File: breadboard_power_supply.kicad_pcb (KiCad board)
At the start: 2 copper layers, 75.2 x 54.4 mm, 25 parts, among them J1 PJ-059AH, J10 Conn_01x04, J11 Conn_01x12, J12 Conn_01x04, J13 Conn_01x04, J14 Conn_01x04, J2 Conn_01x07, J3 Conn_01x08, J4 Screw_Terminal_01x06, J5 Conn_01x04_Male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

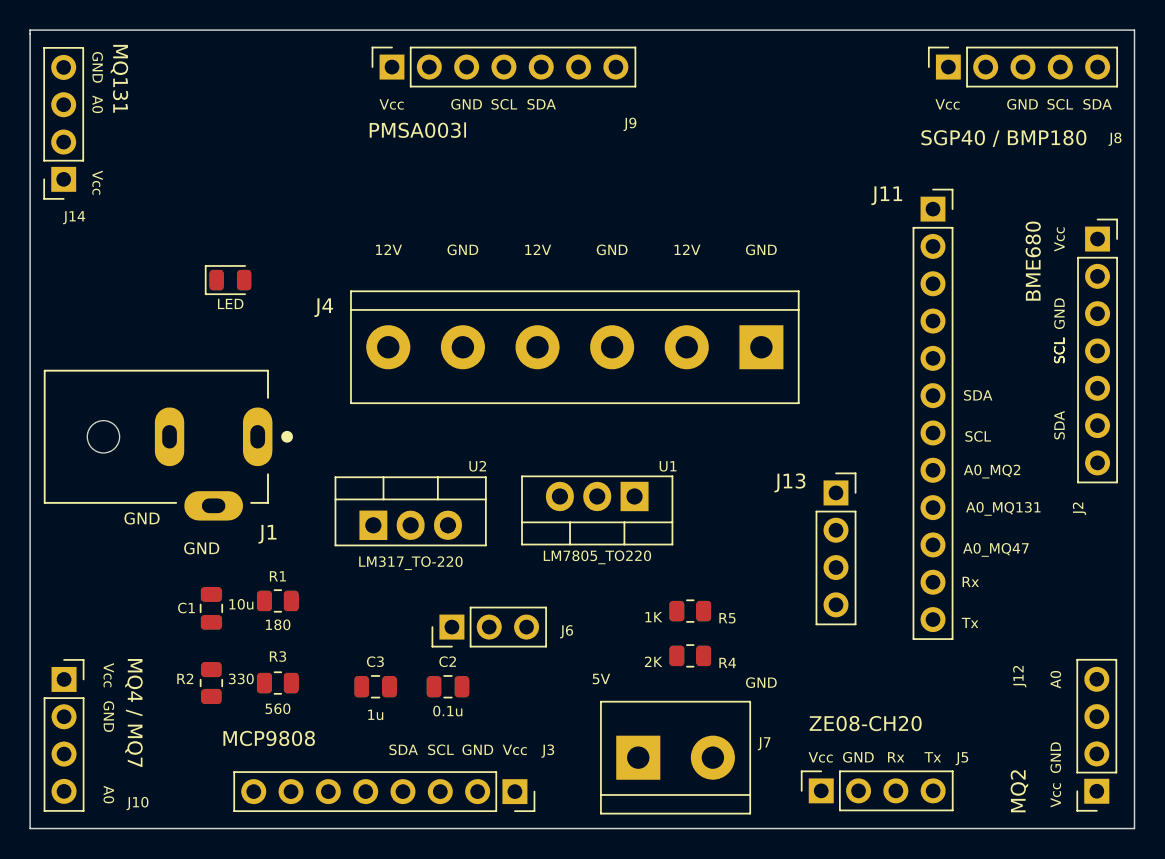
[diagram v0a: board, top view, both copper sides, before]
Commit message: Remaining : route tracking
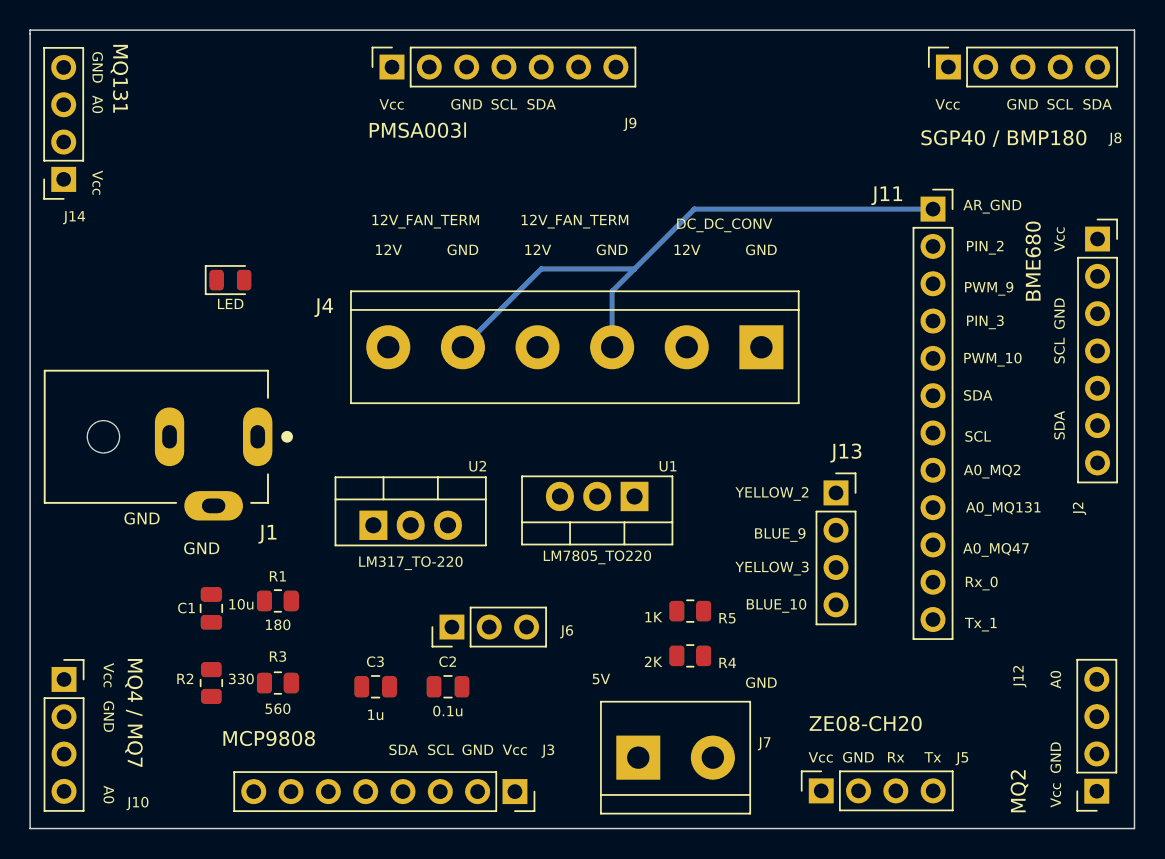
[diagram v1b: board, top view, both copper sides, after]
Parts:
- J11: value Conn_01x12 -> Conn_01x12_Male
- J13: value Conn_01x04 -> Conn_01x04_Male
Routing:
- net GND: track 0.00 -> 41.9 mm
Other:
- board text added: "12V_FAN_TERM"
- board text added: "AR_GND"
- board text added: "BLUE_10"
- board text added: "BLUE_9"
- board text added: "DC_DC_CONV"
- board text added: "PIN_2"
- board text added: "PIN_3"
- board text added: "PWM_10"
- board text added: "PWM_9"
- board text added: "Rx_0"
- board text added: "Tx_1"
- board text added: "YELLOW_2"
- board text added: "YELLOW_3"
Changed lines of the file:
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@@
       (effects (font (size 1 1) (thickness 0.15)))
     )
-    (fp_text value "Conn_01x12" (at -2.794 22.865 90) (layer "F.Fab")
+    (fp_text value "Conn_01x12_Male" (at -2.794 22.865 90) (layer "F.Fab")
       (effects (font (size 1 1) (thickness 0.15)))
     )
@@
     (property "Sheetname" "")
     (attr through_hole)
-    (fp_text reference "J13" (at -3.048 -0.772) (layer "F.SilkS")
-      (effects (font (size 1 1) (thickness 0.15)))
-    )
-    (fp_text value "Conn_01x04" (at -2.794 3.292 90) (layer "F.Fab")
+    (fp_text reference "J13" (at 0.762 -2.804) (layer "F.SilkS")
+      (effects (font (size 1 1) (thickness 0.15)))
+    )
+    (fp_text value "Conn_01x04_Male" (at 2.54 3.546 90) (layer "F.Fab")
       (effects (font (size 1 1) (thickness 0.15)))
     )
@@
   (gr_line (start 55.372 117.19) (end 55.372 65.628) (layer "User.1") (width 0.15))
   (gr_line (start 56.114 117.19) (end 55.372 117.19) (layer "User.1") (width 0.15))
+  (gr_text "YELLOW_2" (at 91.948 143.256) (layer "F.SilkS")
+    (effects (font (size 0.7 0.7) (thickness 0.1)))
+  )
   (gr_text "SDA" (at 114.046 116.84) (layer "F.SilkS")
     (effects (font (size 0.7 0.7) (thickness 0.1)))
   )
+  (gr_text "YELLOW_3" (at 91.948 148.336) (layer "F.SilkS")
+    (effects (font (size 0.7 0.7) (thickness 0.1)))
+  )
   (gr_text "SCL" (at 105.918 139.446) (layer "F.SilkS")
     (effects (font (size 0.7 0.7) (thickness 0.1)))
@@
     (effects (font (size 0.7 0.7) (thickness 0.1)))
   )
+  (gr_text "12V_FAN_TERM" (at 78.486 124.714) (layer "F.SilkS")
+    (effects (font (size 0.7 0.7) (thickness 0.1)))
+  )
   (gr_text "Vcc" (at 111.506 125.984 90) (layer "F.SilkS")
     (effects (font (size 0.7 0.7) (thickness 0.1)))
   )
   (gr_text "Rx" (at 100.33 161.29) (layer "F.SilkS")
+    (effects (font (size 0.7 0.7) (thickness 0.1)))
+  )
+  (gr_text "12V_FAN_TERM" (at 68.326 124.714) (layer "F.SilkS")
     (effects (font (size 0.7 0.7) (thickness 0.1)))
   )
@@
     (effects (font (size 0.7 0.7) (thickness 0.1)))
   )
-  (gr_text "Tx" (at 105.41 152.146) (layer "F.SilkS")
+  (gr_text "Tx_1" (at 106.172 152.146) (layer "F.SilkS")
     (effects (font (size 0.7 0.7) (thickness 0.1)))
   )
@@
     (effects (font (size 0.7 0.7) (thickness 0.1)))
   )
+  (gr_text "PIN_3" (at 106.426 131.572) (layer "F.SilkS")
+    (effects (font (size 0.7 0.7) (thickness 0.1)))
+  )
+  (gr_text "PIN_2" (at 106.426 126.492) (layer "F.SilkS")
+    (effects (font (size 0.7 0.7) (thickness 0.1)))
+  )
   (gr_text "12V" (at 65.786 126.746) (layer "F.SilkS")
     (effects (font (size 0.7 0.7) (thickness 0.1)))
@@
     (effects (font (size 0.7 0.7) (thickness 0.1)))
   )
+  (gr_text "DC_DC_CONV" (at 88.646 124.968) (layer "F.SilkS")
+    (effects (font (size 0.7 0.7) (thickness 0.1)))
+  )
   (gr_text "GND" (at 111.252 161.29 90) (layer "F.SilkS")
     (effects (font (size 0.7 0.7) (thickness 0.1)))
@@
     (effects (font (size 0.7 0.7) (thickness 0.1)))
   )
+  (gr_text "BLUE_10" (at 92.202 150.876) (layer "F.SilkS")
+    (effects (font (size 0.7 0.7) (thickness 0.1)))
+  )
   (gr_text "GND" (at 97.79 161.29) (layer "F.SilkS")
     (effects (font (size 0.7 0.7) (thickness 0.1)))
@@
     (effects (font (size 0.7 0.7) (thickness 0.1)))
   )
-  (gr_text "Rx" (at 105.41 149.352) (layer "F.SilkS")
+  (gr_text "Rx_0" (at 106.172 149.352) (layer "F.SilkS")
     (effects (font (size 0.7 0.7) (thickness 0.1)))
   )
@@
     (effects (font (size 0.7 0.7) (thickness 0.1)))
   )
+  (gr_text "PWM_9" (at 106.68 129.286) (layer "F.SilkS")
+    (effects (font (size 0.7 0.7) (thickness 0.1)))
+  )
+  (gr_text "AR_GND" (at 106.934 123.698) (layer "F.SilkS")
+    (effects (font (size 0.7 0.7) (thickness 0.1)))
+  )
   (gr_text "5V" (at 80.264 155.956) (layer "F.SilkS")
     (effects (font (size 0.7 0.7) (thickness 0.1)))
   )
   (gr_text "Vcc" (at 95.25 161.29) (layer "F.SilkS")
-    (effects (font (size 0.7 0.7) (thickness 0.1)))
-  )
-  (gr_text "SCL" (at 111.488305 133.579759 90) (layer "F.SilkS")
     (effects (font (size 0.7 0.7) (thickness 0.1)))
   )
@@
     (effects (font (size 0.7 0.7) (thickness 0.1)))
   )
+  (gr_text "BLUE_9" (at 92.456 146.05) (layer "F.SilkS")
+    (effects (font (size 0.7 0.7) (thickness 0.1)))
+  )
   (gr_text "A0" (at 45.974 116.84 270) (layer "F.SilkS")
     (effects (font (size 0.7 0.7) (thickness 0.1)))
   )
   (gr_text "A0_MQ47\n" (at 107.188 147.066) (layer "F.SilkS")
+    (effects (font (size 0.7 0.7) (thickness 0.1)))
+  )
+  (gr_text "PWM_10" (at 106.934 134.112) (layer "F.SilkS")
     (effects (font (size 0.7 0.7) (thickness 0.1)))
   )
@@
     (style (thickness 0.1) (arrow_length 1.27) (text_position_mode 0) (extension_height 0.58642) (extension_offset 0.5) keep_text_aligned)
   )
+  (segment (start 81.026 133.35) (end 81.026 129.54) (width 0.35) (layer "B.Cu") (net 2))
+  (segment (start 76.2 128.016) (end 82.55 128.016) (width 0.35) (layer "B.Cu") (net 2))
+  (segment (start 86.619 123.947) (end 102.87 123.947) (width 0.35) (layer "B.Cu") (net 2))
+  (segment (start 81.026 129.54) (end 82.55 128.016) (width 0.35) (layer "B.Cu") (net 2))
+  (segment (start 82.55 128.016) (end 86.619 123.947) (width 0.35) (layer "B.Cu") (net 2))
+  (segment (start 70.866 133.35) (end 76.2 128.016) (width 0.35) (layer "B.Cu") (net 2))
 )

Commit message: Routing and Copper - hatch fills
proceeding
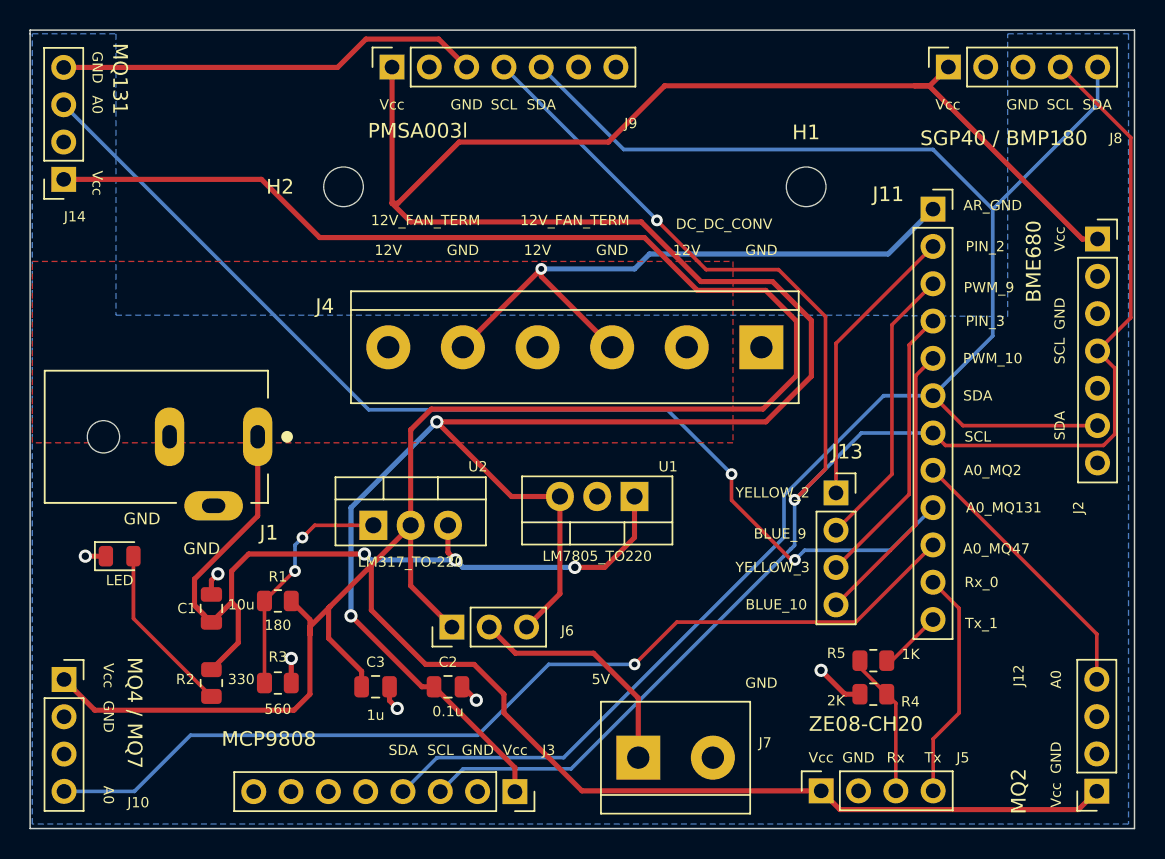
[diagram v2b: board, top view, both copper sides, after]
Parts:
- added H1: MountingHole, MountingHole:MountingHole_2.7mm, F.Cu at (94.2, 122.4)
- added H2: MountingHole, MountingHole:MountingHole_2.7mm, F.Cu at (62.7, 122.4)
- moved D1 20.3 mm to (47.5, 147.6)
- moved R5 12.9 mm to (98.8, 154.7), turned to 180 degrees
- moved R4 12.7 mm to (98.8, 157.0)
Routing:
- net /VCCB: track 0.00 -> 201.0 mm
- net /VCCA: track 0.00 -> 183.2 mm, vias 0 -> 2
- net /SCL: track 0.00 -> 129.2 mm, vias 0 -> 2
- net /SDA: track 0.00 -> 122.7 mm
- net /A0_MQ131: track 0.00 -> 74.5 mm, vias 0 -> 2
- net /A0_MQ47: track 0.00 -> 66.1 mm, vias 0 -> 1
- net /12V: track 0.00 -> 60.4 mm, vias 0 -> 3
- net GND: track 41.9 -> 83.3 mm, vias 0 -> 7
- net /A_WRT_PWM_9: track 0.00 -> 19.5 mm
- net /A_WRT_PWM_10: track 0.00 -> 19.5 mm
- net /INT/PT_PIN_2: track 0.00 -> 19.5 mm
- net /INT/PT_PIN_3: track 0.00 -> 19.5 mm
- net /A0_MQ2: track 0.00 -> 18.8 mm
- net /PWR_OUT: track 0.00 -> 16.2 mm
- net Net-(R1-Pad1): track 0.00 -> 16.2 mm, vias 0 -> 2
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- added copper zone on F.Cu, net /12V
- added copper zone on B.Cu, net GND
